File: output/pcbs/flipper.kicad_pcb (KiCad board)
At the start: 2 copper layers, 147.6 x 106.8 mm, 2 parts

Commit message: output file
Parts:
- removed MH1: , ceoloide:mounting_hole_npth
- added S1, S19: , MX, F.Cu at (109.5, 87.3)
- added S10, S28: , MX, F.Cu at (166.8, 72.8)
- added S11, S29: , MX, F.Cu at (166.8, 53.8)
- added S12, S30: , MX, F.Cu at (166.8, 34.8)
- added S13, S31: , MX, F.Cu at (185.8, 76.0)
- added S14, S32: , MX, F.Cu at (185.8, 57.0)
- added S15, S33: , MX, F.Cu at (185.8, 38.0)
- added S16, S34: , MX, F.Cu at (176.3, 97.5)
- added S17, S35: , MX, F.Cu at (201.5, 94.5)
- added S18, S36: , MX, F.Cu at (217.9, 104.0)
- added S2, S20: , MX, F.Cu at (107.1, 68.5)
- added S21, S3: , MX, F.Cu at (104.8, 49.6)
- added S22, S4: , MX, F.Cu at (128.8, 72.8)
- added S23, S5: , MX, F.Cu at (128.8, 53.8)
- added S24, S6: , MX, F.Cu at (128.8, 34.8)
- added S25, S7: , MX, F.Cu at (147.8, 66.5)
- added S26, S8: , MX, F.Cu at (147.8, 47.5)
- added S27, S9: , MX, F.Cu at (147.8, 28.5)
- MCU1: footprint ProMicro -> ceoloide:mcu_nice_nano
- moved MCU1 57.7 mm to (208.8, 44.9), turned to 0 degrees
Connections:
- MCU1 pad 1: RAW -> MCU1_1
- MCU1 pad 10: P14 -> MCU1_10
- MCU1 pad 11: P16 -> MCU1_11
- MCU1 pad 12: P10 -> MCU1_12
- MCU1 pad 13: P1 -> MCU1_13
- MCU1 pad 14: P0 -> MCU1_14
- MCU1 pad 15: GND -> MCU1_15
- MCU1 pad 16: GND -> MCU1_16
- MCU1 pad 17: P2 -> MCU1_17
- MCU1 pad 18: P3 -> MCU1_18
- MCU1 pad 19: P4 -> MCU1_19
- MCU1 pad 2: GND -> MCU1_2
- MCU1 pad 20: P5 -> MCU1_20
- MCU1 pad 21: P6 -> MCU1_21
- MCU1 pad 22: P7 -> MCU1_22
- MCU1 pad 23: P8 -> MCU1_23
- MCU1 pad 24: P9 -> MCU1_24
- MCU1 pad 3: RST -> MCU1_3
- MCU1 pad 4: VCC -> MCU1_4
- MCU1 pad 5: P21 -> MCU1_5
- MCU1 pad 6: P20 -> MCU1_6
- MCU1 pad 7: P19 -> MCU1_7
- MCU1 pad 8: P18 -> MCU1_8
- MCU1 pad 9: P15 -> MCU1_9
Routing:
- net (no net): track 0.00 -> 337.7 mm

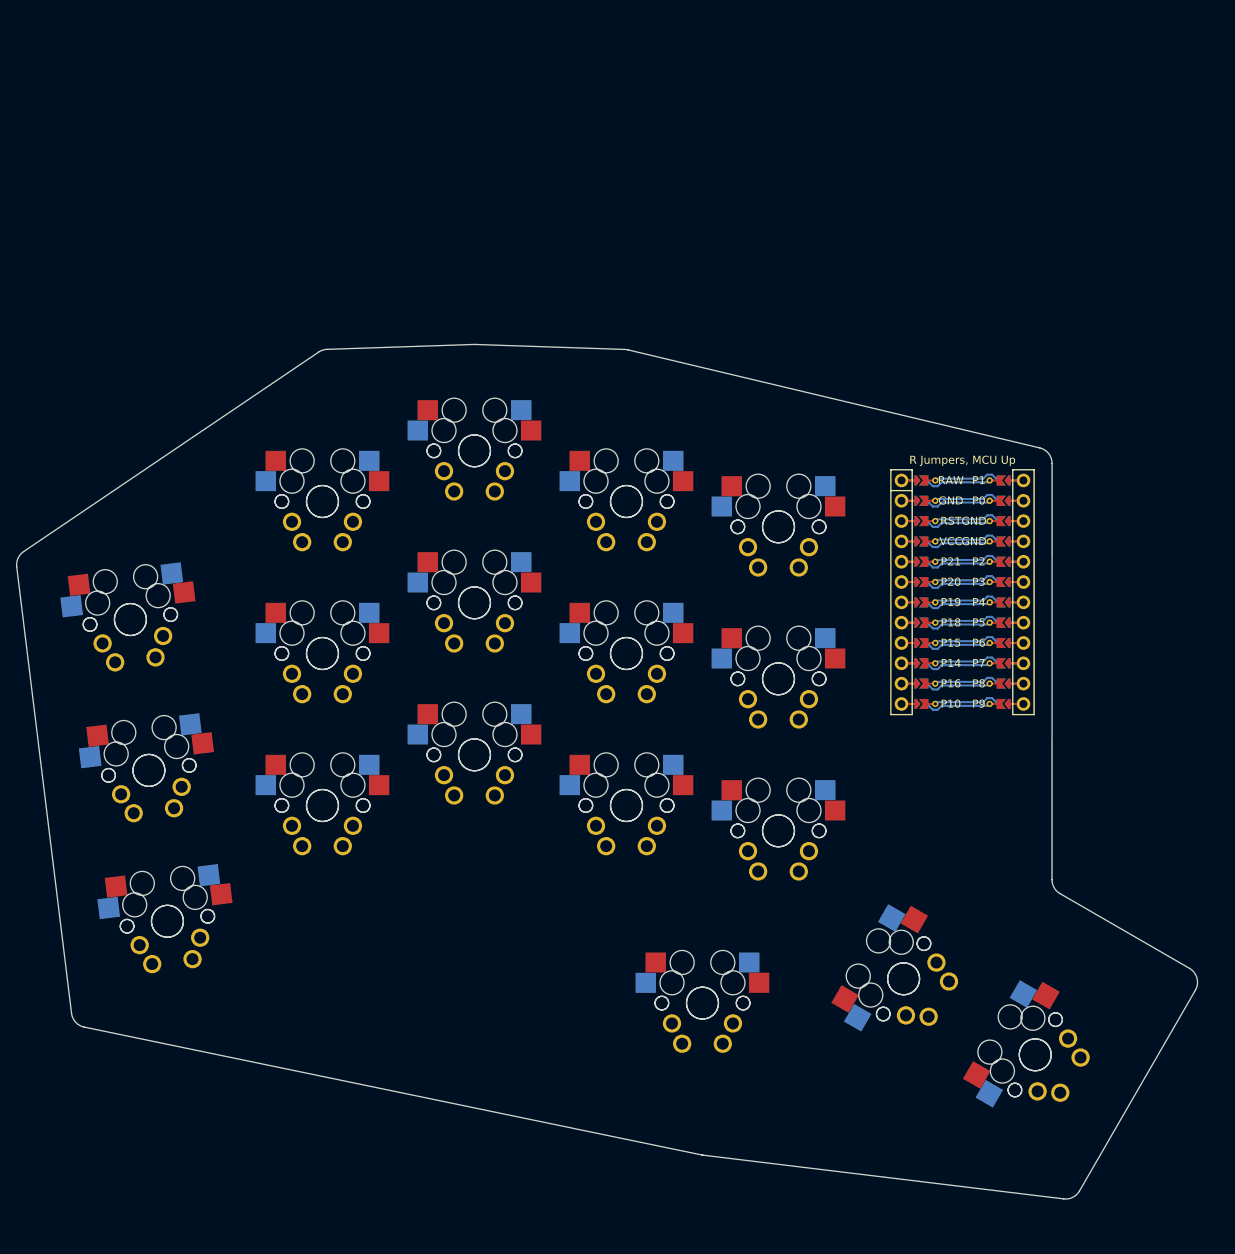
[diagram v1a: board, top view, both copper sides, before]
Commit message: adding diodes and testing on jst
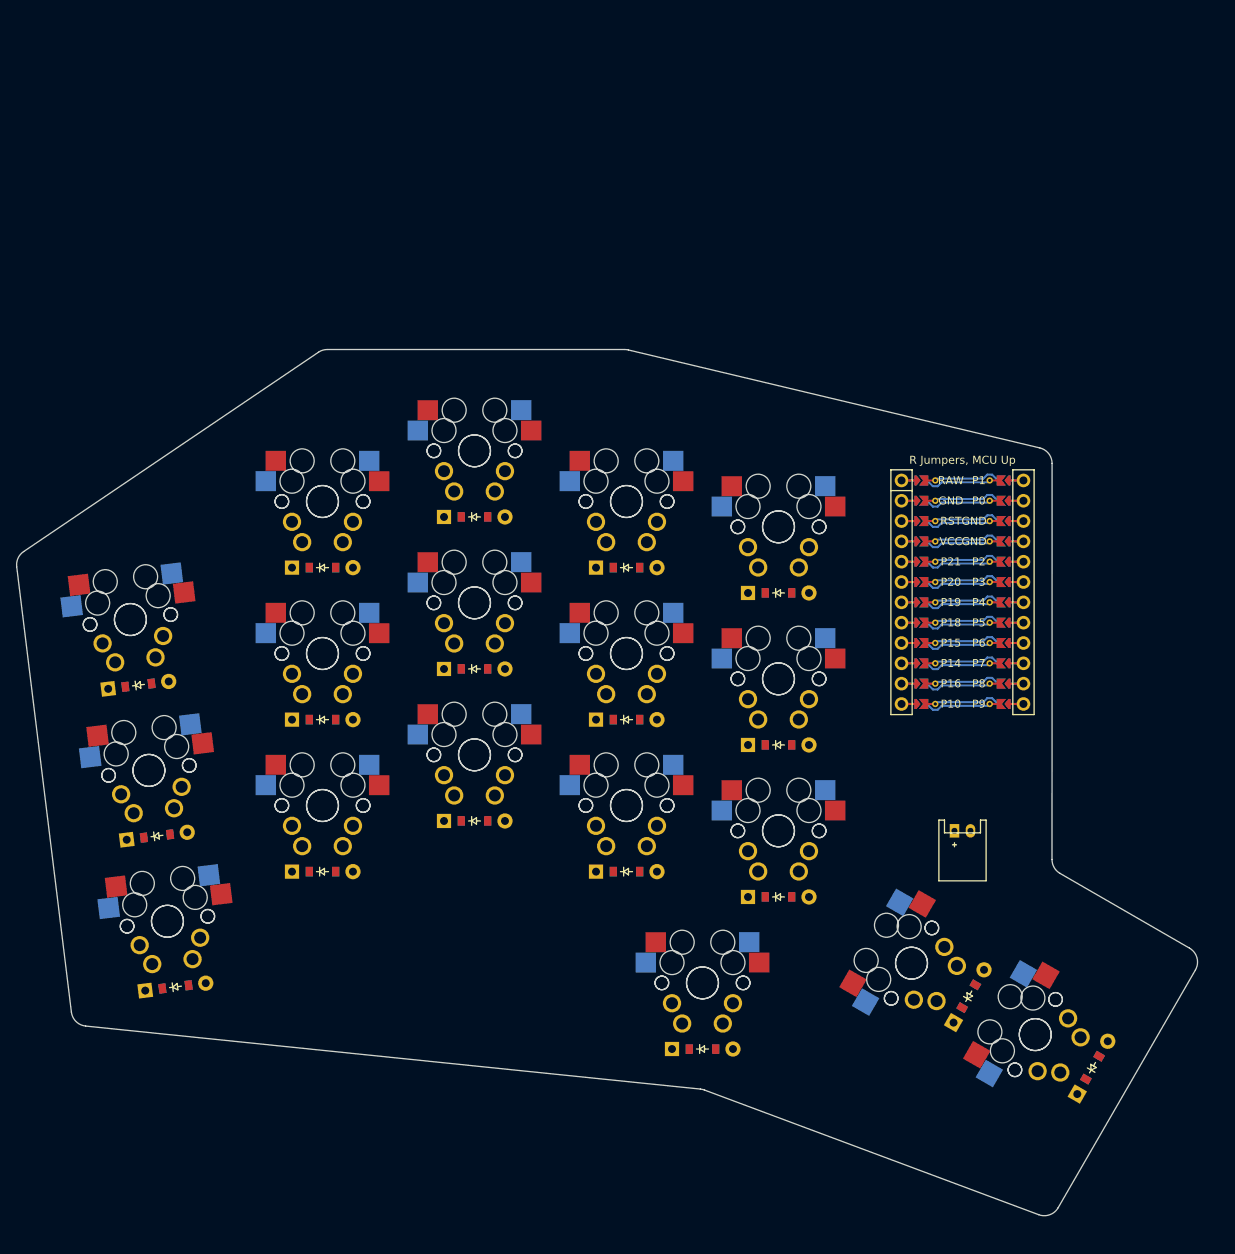
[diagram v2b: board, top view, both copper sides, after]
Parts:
- added D1: , ComboDiode, F.Cu at (110.5, 95.5)
- added D10: , ComboDiode, F.Cu at (166.8, 81.1)
- added D11: , ComboDiode, F.Cu at (166.8, 62.1)
- added D12: , ComboDiode, F.Cu at (166.8, 43.1)
- added D13: , ComboDiode, F.Cu at (185.8, 84.3)
- added D14: , ComboDiode, F.Cu at (185.8, 65.3)
- added D15: , ComboDiode, F.Cu at (185.8, 46.3)
- added D16: , ComboDiode, F.Cu at (176.3, 103.3)
- added D17: , ComboDiode, F.Cu at (209.6, 96.7)
- added D18: , ComboDiode, F.Cu at (225.1, 105.6)
- added D2: , ComboDiode, F.Cu at (108.1, 76.7)
- added D3: , ComboDiode, F.Cu at (105.8, 57.8)
- added D4: , ComboDiode, F.Cu at (128.8, 81.1)
- added D5: , ComboDiode, F.Cu at (128.8, 62.1)
- added D6: , ComboDiode, F.Cu at (128.8, 43.1)
- added D7: , ComboDiode, F.Cu at (147.8, 74.8)
- added D8: , ComboDiode, F.Cu at (147.8, 55.8)
- added D9: , ComboDiode, F.Cu at (147.8, 36.8)
- added JST1: , JST_PH_S2B-PH-K_02x2.00mm_Angled, F.Cu at (208.8, 76.0)
- moved S16 2.53 mm to (176.3, 95.0)
- moved S18 2.53 mm to (217.9, 101.5)
- moved S34 2.53 mm to (176.3, 95.0)
- moved S36 2.53 mm to (217.9, 101.5)
- moved S17 2.19 mm to (202.5, 92.5)
- moved S35 2.19 mm to (202.5, 92.5)
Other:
- board size 147.6 x 106.8 mm -> 147.6 x 108.3 mm

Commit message: added external footprints
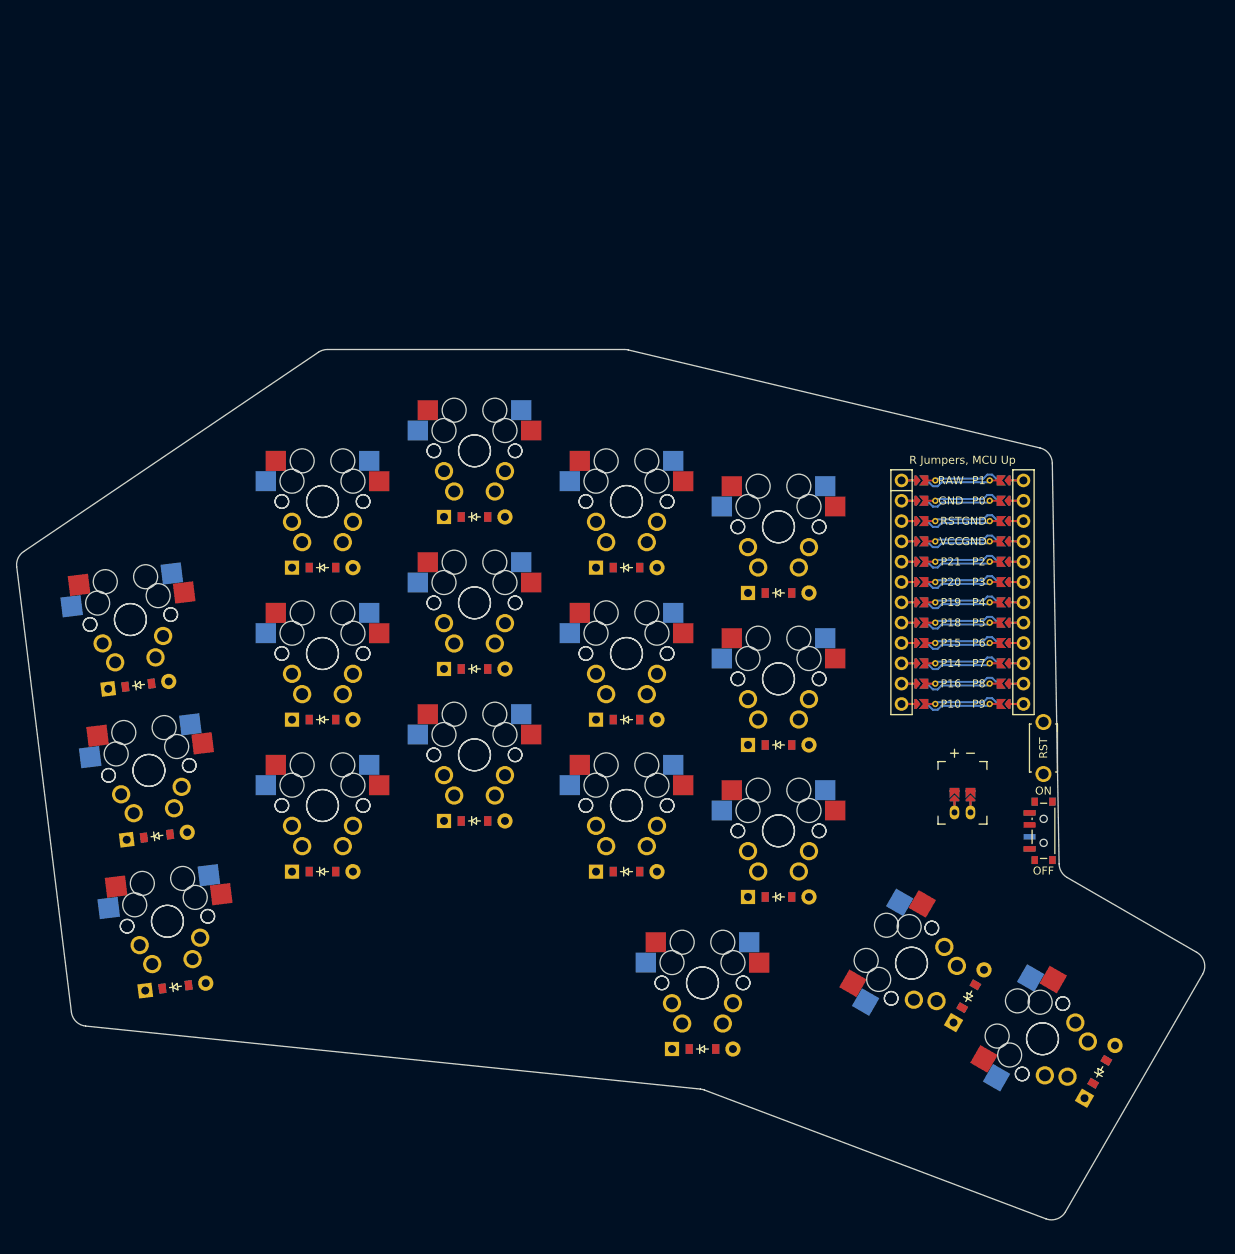
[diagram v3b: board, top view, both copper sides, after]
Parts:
- added PWR1: , ceoloide:power_switch_smd_side, F.Cu at (219.0, 76.0)
- added RST1: , ceoloide:reset_switch_tht_top, F.Cu at (219.0, 65.7)
- JST1: footprint JST_PH_S2B-PH-K_02x2.00mm_Angled -> ceoloide:battery_connector_jst_ph_2
- moved JST1 2.30 mm to (208.8, 73.7), turned to 180 degrees
- moved S18 1.04 mm to (218.8, 102.0)
- moved S36 1.04 mm to (218.8, 102.0)
- moved D18 1.04 mm to (226.0, 106.1)
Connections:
- D1 pad 1: P18 -> P10
- D10 pad 1: P18 -> P10
- D11 pad 1: (no net) -> P16
- D12 pad 1: (no net) -> P14
- D13 pad 1: P18 -> P10
- D14 pad 1: (no net) -> P16
- D15 pad 1: (no net) -> P14
- D16 pad 1: (no net) -> P9
- D17 pad 1: (no net) -> P9
- D18 pad 1: (no net) -> P9
- D2 pad 1: (no net) -> P16
- D3 pad 1: (no net) -> P14
- D4 pad 1: P18 -> P10
- D5 pad 1: (no net) -> P16
- D6 pad 1: (no net) -> P14
- D7 pad 1: P18 -> P10
- D8 pad 1: (no net) -> P16
- D9 pad 1: (no net) -> P14
- JST1 pad 1: RAW -> BAT_P
- S1 pad 1: P16 -> P21
- S10 pad 1: (no net) -> P18
- S11 pad 1: (no net) -> P18
- S12 pad 1: (no net) -> P18
- S13 pad 1: (no net) -> P15
- S14 pad 1: (no net) -> P15
- S15 pad 1: (no net) -> P15
- S16 pad 1: (no net) -> P19
- S17 pad 1: (no net) -> P18
- S18 pad 1: (no net) -> P15
- S19 pad 1: P16 -> P21
- S2 pad 1: P16 -> P21
- S20 pad 1: P16 -> P21
- S21 pad 1: P16 -> P21
- S22 pad 1: (no net) -> P20
- S23 pad 1: (no net) -> P20
- S24 pad 1: (no net) -> P20
- S25 pad 1: (no net) -> P19
- S26 pad 1: (no net) -> P19
- S27 pad 1: (no net) -> P19
- S28 pad 1: (no net) -> P18
- S29 pad 1: (no net) -> P18
- S3 pad 1: P16 -> P21
- S30 pad 1: (no net) -> P18
- S31 pad 1: (no net) -> P15
- S32 pad 1: (no net) -> P15
- S33 pad 1: (no net) -> P15
- S34 pad 1: (no net) -> P19
- S35 pad 1: (no net) -> P18
- S36 pad 1: (no net) -> P15
- S4 pad 1: (no net) -> P20
- S5 pad 1: (no net) -> P20
- S6 pad 1: (no net) -> P20
- S7 pad 1: (no net) -> P19
- S8 pad 1: (no net) -> P19
- S9 pad 1: (no net) -> P19
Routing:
- net JST1_2: track 0.00 -> 3.60 mm
- net JST1_1: track 0.00 -> 3.60 mm
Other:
- board size 147.6 x 108.3 mm -> 148.5 x 108.8 mm

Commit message: resize
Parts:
- moved RST1 35.3 mm to (219.1, 30.4)
- moved PWR1 32.3 mm to (219.1, 43.7)
- moved JST1 13.0 mm to (218.1, 64.6), turned to -90 degrees
- moved MCU1 4.02 mm to (205.4, 42.8)
- moved D18 0.86 mm to (226.7, 106.6)
- moved S18 0.86 mm to (219.6, 102.4)
- moved S36 0.86 mm to (219.6, 102.4)
- moved S17 0.76 mm to (203.1, 92.9)
- moved S35 0.76 mm to (203.1, 92.9)
- moved D17 0.76 mm to (210.3, 97.1)
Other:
- board size 148.5 x 108.8 mm -> 150.2 x 111 mm

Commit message: adding optional key
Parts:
- added S37, S38: , MX, F.Cu at (208.2, 84.9)
- moved D17 0.38 mm to (210.6, 97.3)
- moved S17 0.38 mm to (203.5, 93.1)
- moved S35 0.38 mm to (203.5, 93.1)
- moved D18 0.38 mm to (227.1, 106.8)
- moved S18 0.38 mm to (219.9, 102.6)
- moved S36 0.38 mm to (219.9, 102.6)
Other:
- board size 150.2 x 111 mm -> 149.6 x 110.4 mm
